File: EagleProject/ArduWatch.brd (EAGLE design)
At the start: 35.5 x 42.2 mm, 31 parts, among them IC1 DS1307Z, IC2 MCP73831, J1 FTS-105-01-L-D, Q1 32.768Hz, U2 ATMEGA328P-AU

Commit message: Starting Schematic
Starting Schematic in Eagle
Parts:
- LED1: value (none) -> Red
- LED2: value (none) -> Green
- moved IC1 36.6 mm to (25.4, 24.1), turned to 90 degrees
- moved U2 7.73 mm to (10.2, 24.1)
- moved J1 1.80 mm to (20.3, 3.81)
- renumbered PAD1 to USB+, PAD2 to USB-, PAD3 to BATTERY+, PAD4 to BATTERY-
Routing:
- added copper zone on layer 1, net GND

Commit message: Schematic V0.2.0
Schematic version 0.2.0
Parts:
- removed BATTERY+, BATTERY-: WIREPAD2,54/0,8, wirepad:2,54/0,8
- removed C4: 100nF, Kemet_By_element14_Batch_1:CAPC3216X88N
- removed H1, H2, H3, H4: MOUNT-HOLE3.0, holes:3,0
- removed LED2: Green, adafruit:CHIPLED_1206
- removed R5: 10K Ohms, Multicomp_By_element14_Batch_1:RESC3216X71N
- removed R6: 4.7 KOhm, Panasonic_By_element14_Batch_1:RESC3216X71N
- removed U$1: BATERY3,7V, Podreczne:BATERY3,7V
- removed U2: ATMEGA328P-AU, Atmel_By_element14_Batch_1-00:QFP80P900X900X120-32N
- added B+, B-: WIREPAD2,54/0,8, wirepad:2,54/0,8
- added C5: 0.1µF, AVX_By_element14_Batch_1:CAPC3216X94N
- added U1: ATMEGA328P_TQFP, SparkFun-DigitalIC:TQFP32-08
- S1: value (none) -> Button1
- S2: value (none) -> Button2
- moved R7 175.7 mm to (15.4, 13.6), turned to 270 degrees
- moved R4 140.6 mm to (21.6, 20.7)
- moved R3 128.7 mm to (21.6, 18.4)
- moved C3 106.1 mm to (3.81, 20.1)
- moved C2 98.5 mm to (3.81, 22.5)
- moved C1 93.9 mm to (7.62, 26.9), turned to 180 degrees
- moved R2 77.0 mm to (10.2, 18.4), turned to 270 degrees
- moved R1 71.1 mm to (10.2, 22.2)
- moved LED1 47.6 mm to (6.73, 24.8), turned to 270 degrees
- moved USB+ 40.9 mm to (2.54, 26.0)
- moved USB- 36.9 mm to (2.54, 16.5)
- moved H5 30.5 mm to (2.54, 33.0)
- moved IC2 30.1 mm to (7.62, 18.4), turned to 180 degrees
- moved IC1 11.3 mm to (22.2, 13.3), turned to 0 degrees
- moved Q1 7.62 mm to (14.0, 8.89), flipped to the bottom
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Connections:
- removed net AVCC: U2.18
- removed net N$7: LED2.A, R6.2
- removed net SQW: IC1.7, LED2.C, R5.2
- removed net VCC_2: U2.4
- new net D10: 1,3"OLED1.CS, U1.14
- new net D8: 1,3"OLED1.RST, U1.12
- new net D9: 1,3"OLED1.DC, U1.13
- net BUTTON1: now also U1.32
- net BUTTON2: now also U1.1
- net D11: now also 1,3"OLED1.D1, U1.15
- net D12: now also U1.16
- net D13: now also 1,3"OLED1.D0, U1.17
- net GND: now also B-.1, C5.1, U1.21, U1.3, U1.5; no longer BATTERY-.1, C4.1, R6.1, U$1.-
- net N$2: now also Q1.2; no longer Q1.1
- net N$5: now also Q1.1; no longer Q1.2
- net RESET: now also U1.29; no longer U2.29
- net SCL: now also U1.28
- net SDA: now also U1.27
- net VCC: now also B+.1, C5.2, U1.18, U1.23, U1.4, U1.6; no longer BATTERY+.1, C4.2, R5.1, U$1.+, U2.6
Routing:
- net VCC: track 0.00 -> 87.3 mm
- net D11: track 0.00 -> 69.6 mm, vias 0 -> 2
- net GND: track 0.00 -> 68.4 mm, vias 0 -> 4
- net BUTTON1: track 0.00 -> 53.9 mm
- net D13: track 0.00 -> 48.2 mm, vias 0 -> 4
- net D12: track 0.00 -> 48.1 mm, vias 0 -> 2
- net RESET: track 0.00 -> 40.0 mm, vias 0 -> 2
- net BUTTON2: track 0.00 -> 36.5 mm
- net SCL: track 0.00 -> 17.9 mm
- net D10: track 0.00 -> 14.4 mm
- net D9: track 0.00 -> 12.3 mm
- net VUSB: track 0.00 -> 12.2 mm
- net SDA: track 0.00 -> 11.5 mm
- net D8: track 0.00 -> 10.1 mm
- net N$5: track 0.00 -> 9.99 mm
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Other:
- board size 35.5 x 42.2 mm -> 35.5 x 42.5 mm

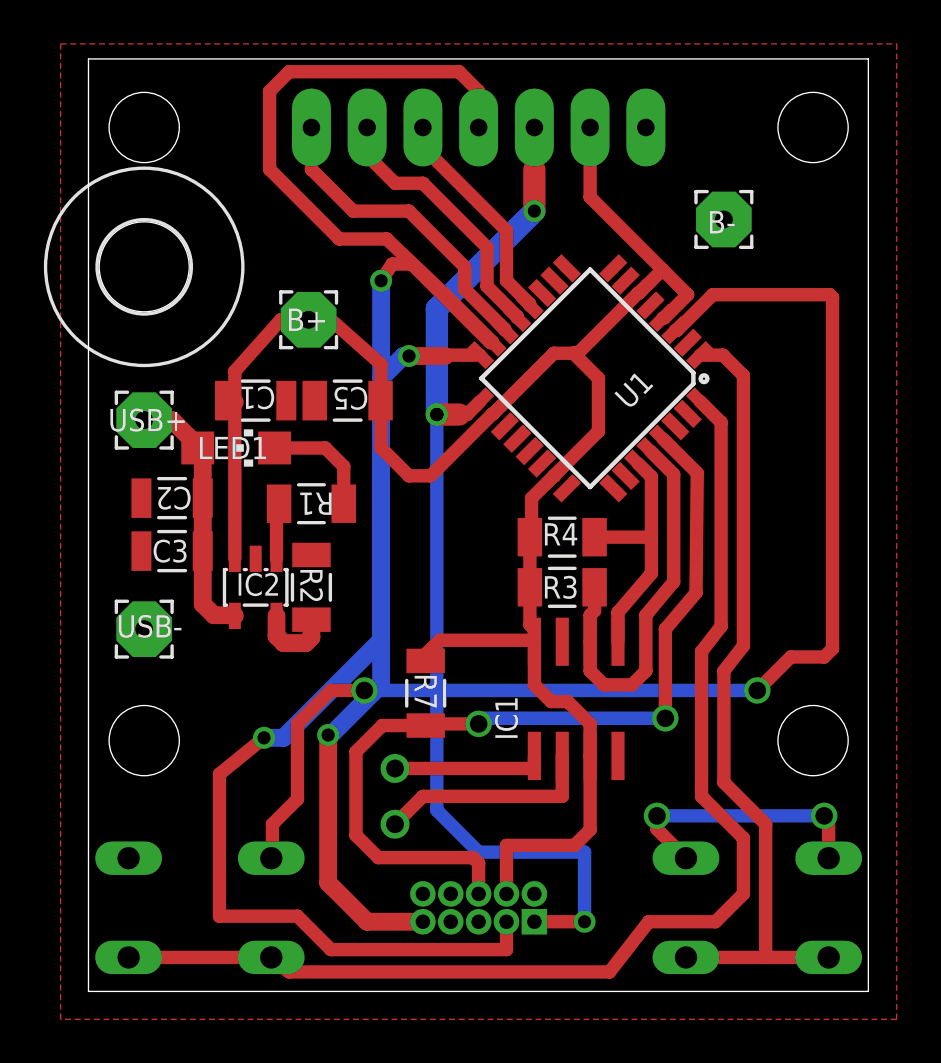
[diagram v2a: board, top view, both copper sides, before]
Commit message: Board V0.1.0
Update board to version 0.1.0
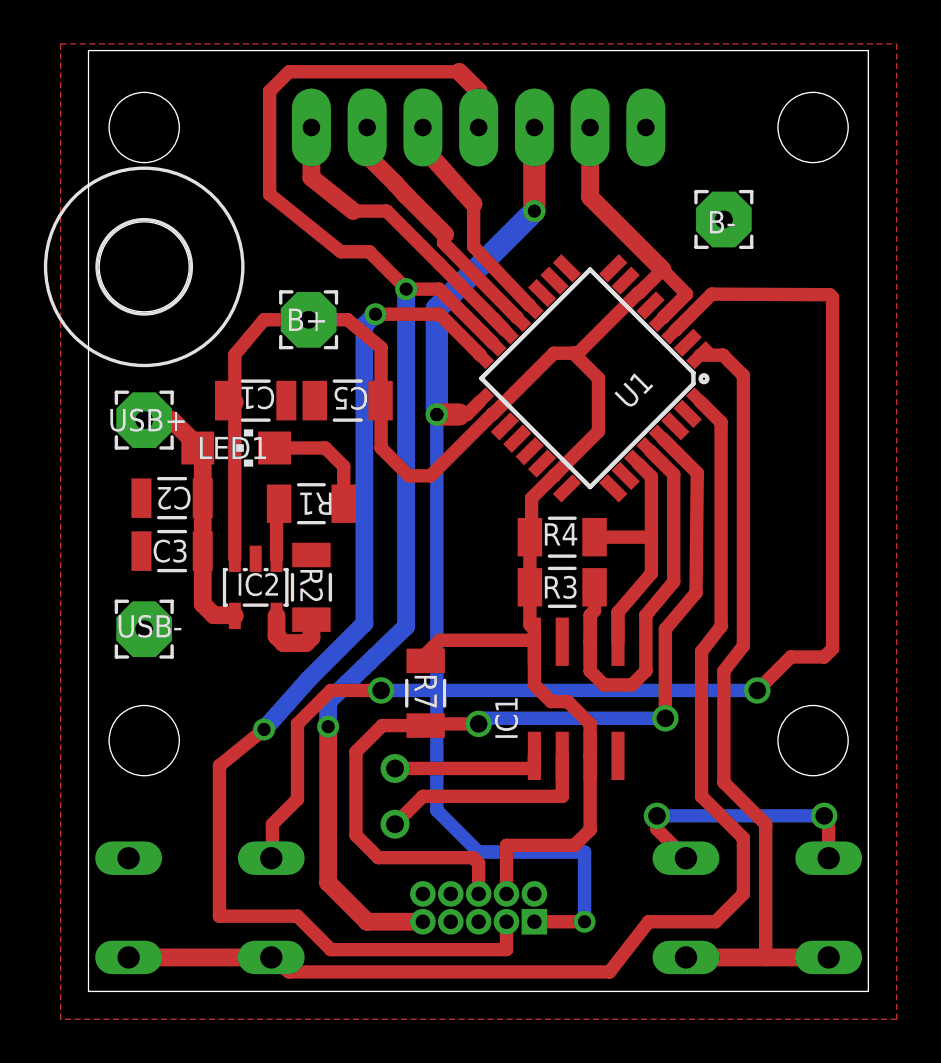
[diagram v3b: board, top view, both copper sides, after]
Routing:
- net D11: track 69.6 -> 63.0 mm
- net D12: track 48.1 -> 51.0 mm
- net VCC: track 87.3 -> 88.1 mm
- net D9: track 12.3 -> 11.5 mm
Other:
- board size 35.5 x 42.5 mm -> 35.5 x 42.9 mm
